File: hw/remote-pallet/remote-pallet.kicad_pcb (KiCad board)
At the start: 2 copper layers, 74 parts, among them M0 E-MATCH, M1 E-MATCH, M2 E-MATCH, M3 E-MATCH, M4 E-MATCH, M5 E-MATCH, M6 E-MATCH, M7 E-MATCH, Q1 Q_PMOS_DGS, Q10 Q_PMOS_DGS, Q11 Q_NMOS_DGS, Q12 Q_PMOS_DGS, Q13 Q_NMOS_DGS, Q14 Q_PMOS_DGS, Q15 Q_NMOS_DGS, Q16 Q_PMOS_DGS, Q17 Q_NMOS_DGS, Q2 Q_PMOS_DGS, Q3 Q_NMOS_DGS, Q4 Q_PMOS_DGS, Q5 Q_NMOS_DGS, Q6 Q_PMOS_DGS, Q7 Q_NMOS_DGS, Q8 Q_PMOS_DGS, Q9 Q_NMOS_DGS, SW1 Power, SW2 Arm Hardware, U1 LM1084IS-3.3/NOPB, U2 PHOTON, U3 LM1084IS-3.3/NOPB

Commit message: updating schematic and pcb
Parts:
- D1, D10, D11, D12, D13, D14, D15, D16, D2, D3, D4, D5, D6, D7, D8, D9, R12, R15, R18, R21, R24, R27, R30, R9: moved to B.Cu
- Q1: value Q_PMOS_DGS -> EMatch Test; footprint TO_SOT_Packages_SMD:TO-252-2Lead -> TO_SOT_Packages_SMD:SOT-23
- U1: value LM1084IS-3.3/NOPB -> Photon Power
- U3: value LM1084IS-3.3/NOPB -> Armed Sense
- moved D10 217.0 mm to (3.81, 194.3)
- moved D4 214.7 mm to (3.81, 203.2)
- moved D12 214.5 mm to (3.81, 189.2)
- moved D6 212.0 mm to (3.81, 199.4)
- moved D14 207.3 mm to (3.81, 185.4)
- moved D16 200.4 mm to (3.81, 179.1)
- moved R32 189.4 mm to (14.0, 43.2), turned to 90 degrees
- moved R31 185.2 mm to (16.5, 43.2), turned to 270 degrees
- moved R29 178.5 mm to (14.0, 57.1), turned to 90 degrees
- moved R28 171.5 mm to (16.5, 57.1), turned to 90 degrees
- moved D2 169.9 mm to (5.08, 174.0)
- moved R22 141.6 mm to (16.5, 83.8), turned to 90 degrees
- moved R20 137.2 mm to (53.3, 36.8), turned to 270 degrees
- moved R9 135.1 mm to (44.5, 205.7)
- moved R26 128.9 mm to (14.0, 69.8), turned to 90 degrees
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
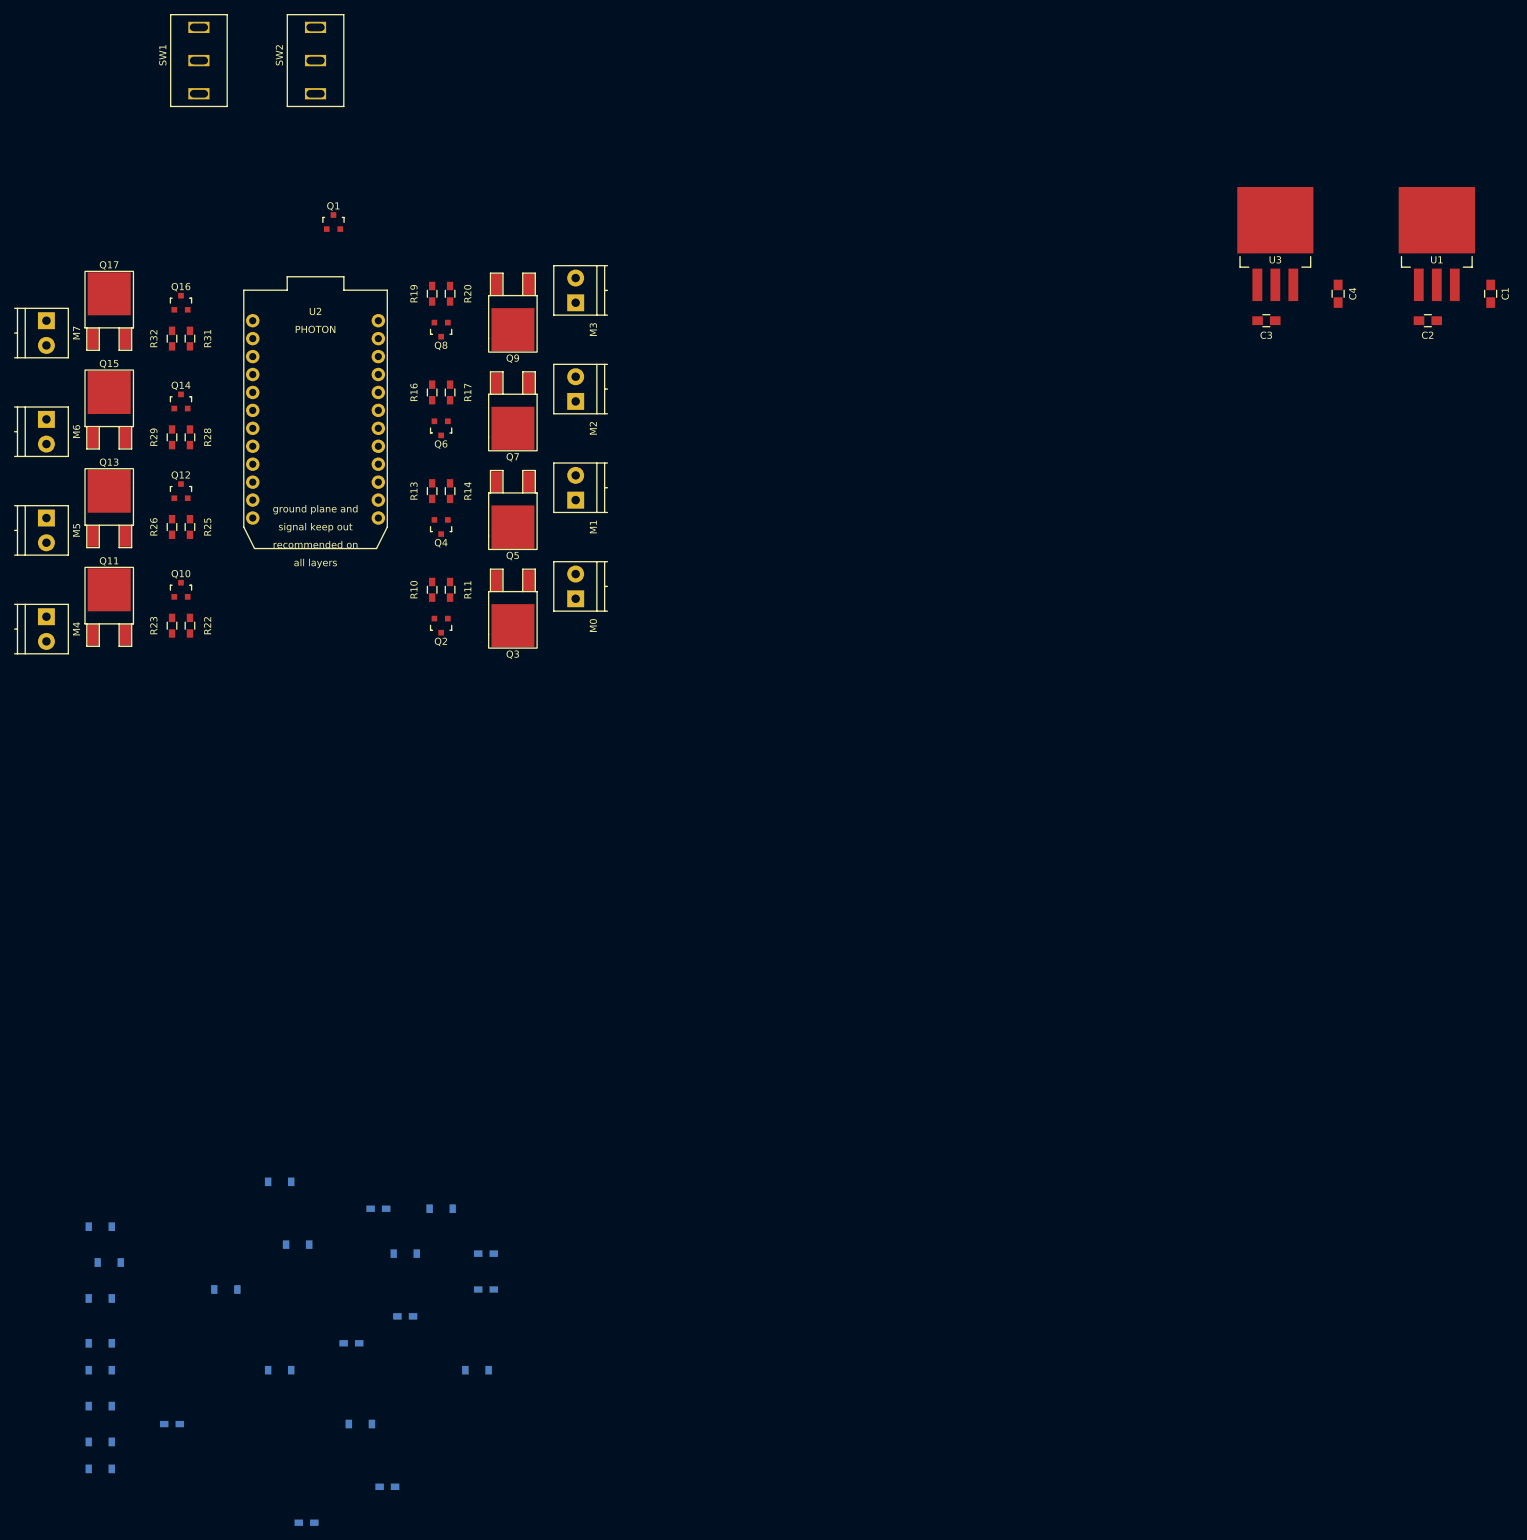
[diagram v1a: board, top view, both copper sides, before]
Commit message: adding some new footprints, laying out board
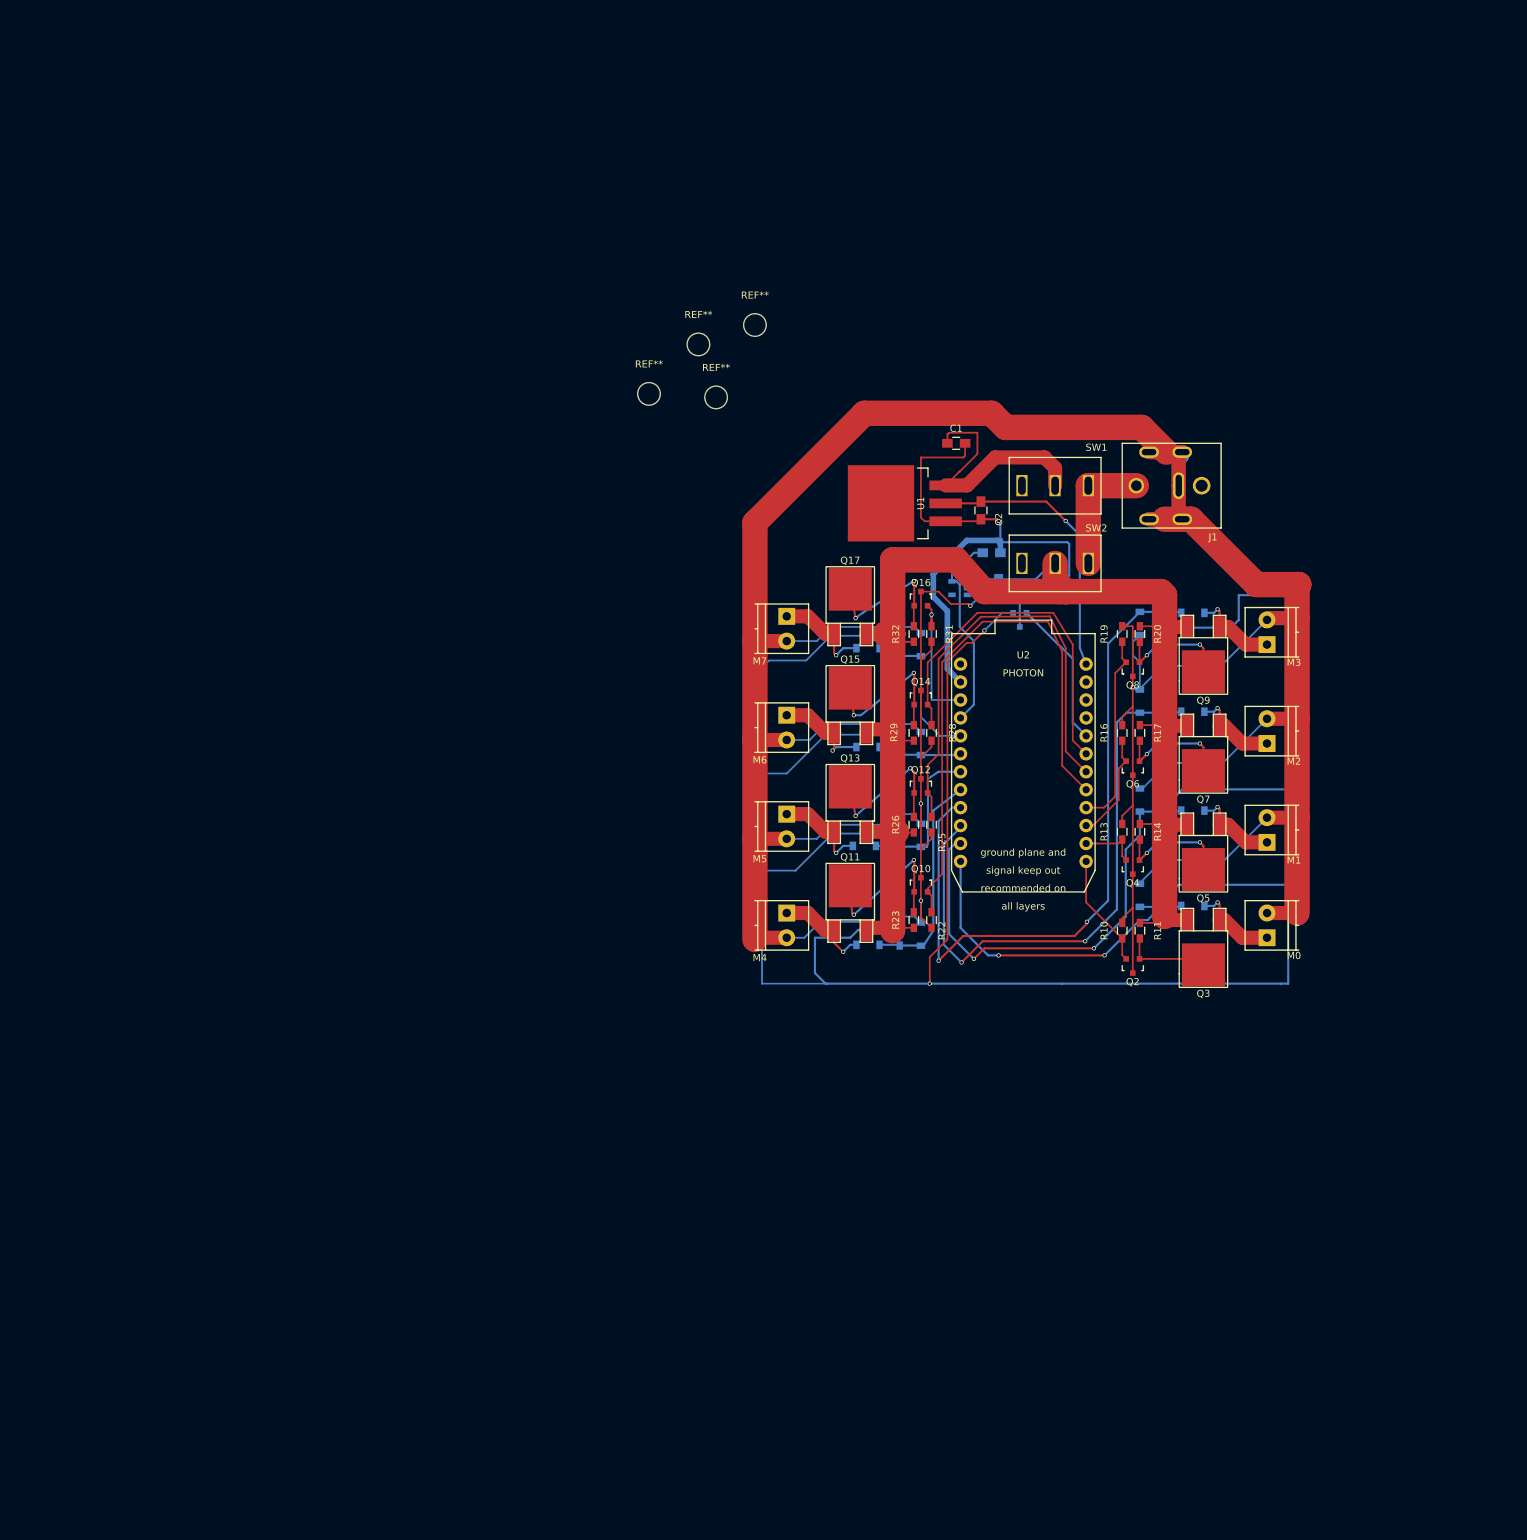
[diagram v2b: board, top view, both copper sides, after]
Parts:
- added J1: Power, PJ-082BH-Barrel-Connector:PJ-082BH-Barrel-Connector, F.Cu at (162.5, 64.0)
- added REF**: MountingHole_3.2mm_M3, Mounting_Holes:MountingHole_3.2mm_M3, F.Cu at (81.5, 51.0)
- added REF**: MountingHole_3.2mm_M3, Mounting_Holes:MountingHole_3.2mm_M3, F.Cu at (88.5, 44.0)
- added REF**: MountingHole_3.2mm_M3, Mounting_Holes:MountingHole_3.2mm_M3, F.Cu at (96.5, 41.2)
- added REF**: MountingHole_3.2mm_M3, Mounting_Holes:MountingHole_3.2mm_M3, F.Cu at (91.0, 51.5)
- C3: value 10uF -> 0.47uF; moved to B.Cu
- C4, Q1: moved to B.Cu
- U3: footprint TO_SOT_Packages_SMD:TO-263-3Lead -> TO_SOT_Packages_SMD:SOT-23-5; moved to B.Cu
- moved D6 186.1 mm to (158.5, 96.0), turned to 180 degrees
- moved D4 180.6 mm to (158.5, 110.0), turned to 180 degrees
- moved D2 161.5 mm to (158.5, 123.5), turned to 180 degrees
- moved D7 160.1 mm to (151.0, 83.5), turned to 270 degrees
- moved D8 155.1 mm to (158.5, 82.0), turned to 180 degrees
- moved D1 154.5 mm to (151.0, 122.0), turned to 90 degrees
- moved R30 150.6 mm to (117.0, 87.0), turned to 90 degrees
- moved R18 145.5 mm to (154.0, 83.0), turned to 270 degrees
- moved D16 142.4 mm to (112.5, 87.0)
- moved D3 141.4 mm to (151.0, 108.5), turned to 90 degrees
- moved D14 137.6 mm to (112.5, 101.0)
- moved R9 137.6 mm to (154.0, 122.5), turned to 90 degrees
- moved SW1 135.3 mm to (139.0, 64.0), turned to 90 degrees
- moved D5 133.3 mm to (151.0, 94.5), turned to 90 degrees
- moved D12 131.2 mm to (112.0, 115.0)
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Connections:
- C4 pad 1: /ematch-0/EMATCH_VCC -> /ematch-0/VCC
- D10 pad 1: /ematch-0/EMATCH_VCC -> /ematch-4/EMATCH_VCC
- D12 pad 1: /ematch-0/EMATCH_VCC -> /ematch-5/EMATCH_VCC
- D14 pad 1: /ematch-0/EMATCH_VCC -> /ematch-6/EMATCH_VCC
- D16 pad 1: /ematch-0/EMATCH_VCC -> /ematch-7/EMATCH_VCC
- D4 pad 1: /ematch-0/EMATCH_VCC -> /ematch-1/EMATCH_VCC
- D6 pad 1: /ematch-0/EMATCH_VCC -> /ematch-2/EMATCH_VCC
- D8 pad 1: /ematch-0/EMATCH_VCC -> /ematch-3/EMATCH_VCC
- M1 pad 1: /ematch-0/EMATCH_VCC -> /ematch-1/EMATCH_VCC
- M2 pad 1: /ematch-0/EMATCH_VCC -> /ematch-2/EMATCH_VCC
- M3 pad 1: /ematch-0/EMATCH_VCC -> /ematch-3/EMATCH_VCC
- M4 pad 1: /ematch-0/EMATCH_VCC -> /ematch-4/EMATCH_VCC
- M5 pad 1: /ematch-0/EMATCH_VCC -> /ematch-5/EMATCH_VCC
- M6 pad 1: /ematch-0/EMATCH_VCC -> /ematch-6/EMATCH_VCC
- M7 pad 1: /ematch-0/EMATCH_VCC -> /ematch-7/EMATCH_VCC
- Q11 pad 1: /ematch-0/EMATCH_VCC -> /ematch-4/EMATCH_VCC
- Q11 pad 3: 12V -> /ematch-0/VCC
- Q13 pad 1: /ematch-0/EMATCH_VCC -> /ematch-5/EMATCH_VCC
- Q13 pad 3: 12V -> /ematch-0/VCC
- Q15 pad 1: /ematch-0/EMATCH_VCC -> /ematch-6/EMATCH_VCC
- Q15 pad 3: 12V -> /ematch-0/VCC
- Q17 pad 1: /ematch-0/EMATCH_VCC -> /ematch-7/EMATCH_VCC
- Q17 pad 3: 12V -> /ematch-0/VCC
- Q3 pad 3: 12V -> /ematch-0/VCC
- Q5 pad 1: /ematch-0/EMATCH_VCC -> /ematch-1/EMATCH_VCC
- Q5 pad 3: 12V -> /ematch-0/VCC
- Q7 pad 1: /ematch-0/EMATCH_VCC -> /ematch-2/EMATCH_VCC
- Q7 pad 3: 12V -> /ematch-0/VCC
- Q9 pad 1: /ematch-0/EMATCH_VCC -> /ematch-3/EMATCH_VCC
- Q9 pad 3: 12V -> /ematch-0/VCC
- R11 pad 1: 12V -> /ematch-0/VCC
- R14 pad 1: 12V -> /ematch-0/VCC
- R17 pad 1: 12V -> /ematch-0/VCC
- R20 pad 1: 12V -> /ematch-0/VCC
- R23 pad 1: 12V -> /ematch-0/VCC
- R26 pad 1: 12V -> /ematch-0/VCC
- R29 pad 1: 12V -> /ematch-0/VCC
- R32 pad 1: 12V -> /ematch-0/VCC
- SW2 pad 2: /ematch-0/EMATCH_VCC -> /ematch-0/VCC
- U2 pad 1: Net-(U2-Pad1) -> (no net)
- U2 pad 20: Fire7 -> SenseSwitch
- U2 pad 22: Net-(U2-Pad22) -> (no net)
- U2 pad 23: Net-(U2-Pad23) -> (no net)
- U2 pad 3: SenseSwitch -> Fire7
- U3 pad 1: GND -> /ematch-0/VCC
- U3 pad 2: Armed -> GND
- U3 pad 3: /ematch-0/EMATCH_VCC -> (no net)
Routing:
- net GND: track 0.00 -> 661.1 mm, vias 0 -> 5
- net VCCsense: track 0.00 -> 377.1 mm, vias 0 -> 2
- net /ematch-0/VCC: track 0.00 -> 224.3 mm
- net Sense3: track 0.00 -> 100.0 mm, vias 0 -> 2
- net Sense2: track 0.00 -> 82.7 mm, vias 0 -> 2
- net Fire4: track 0.00 -> 79.5 mm
- net Fire5: track 0.00 -> 65.2 mm
- net Sense1: track 0.00 -> 64.5 mm, vias 0 -> 2
- net 3.3V: track 0.00 -> 51.5 mm, vias 0 -> 1
- net Fire6: track 0.00 -> 51.3 mm
- net Sense0: track 0.00 -> 48.2 mm, vias 0 -> 2
- net Net-(C1-Pad1): track 0.00 -> 35.2 mm
- net Sense4: track 0.00 -> 30.7 mm
- net Armed: track 0.00 -> 28.4 mm
- net Fire3: track 0.00 -> 27.5 mm
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
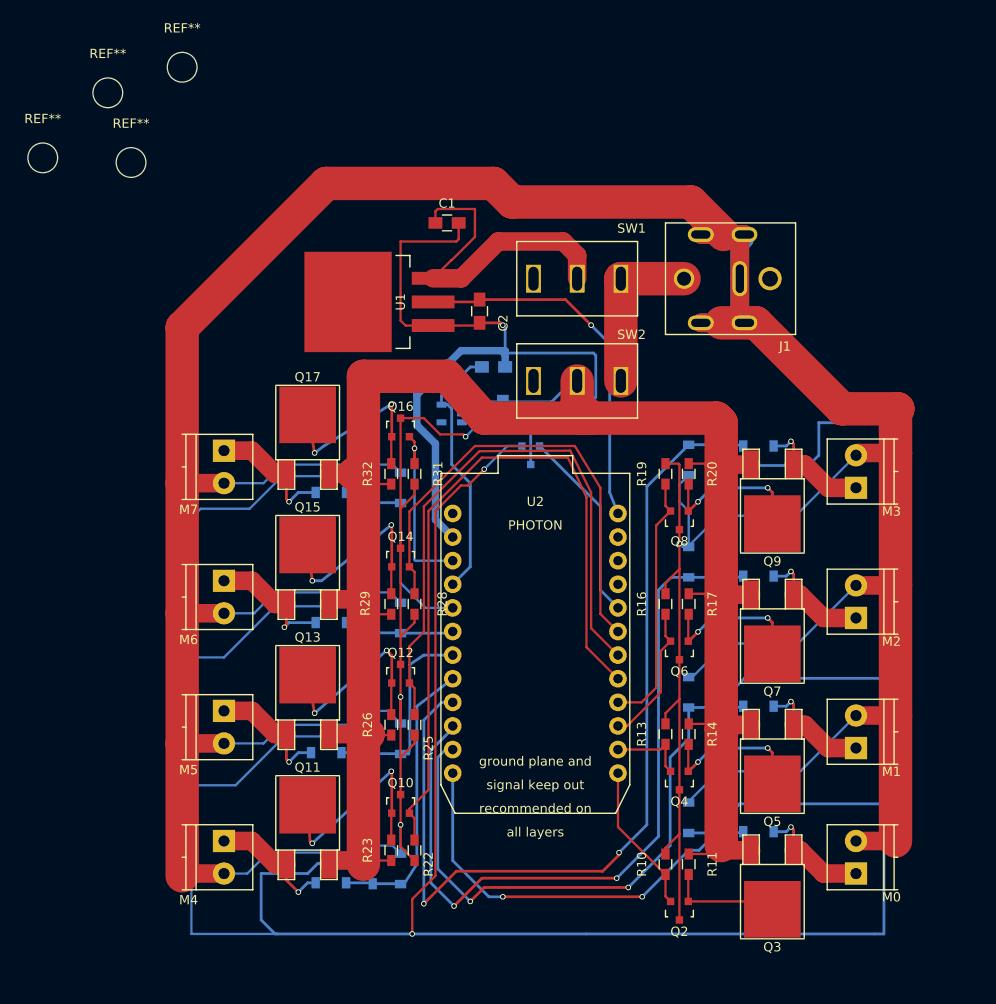
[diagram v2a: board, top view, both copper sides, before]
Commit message: changes to layout adding debug LEDs
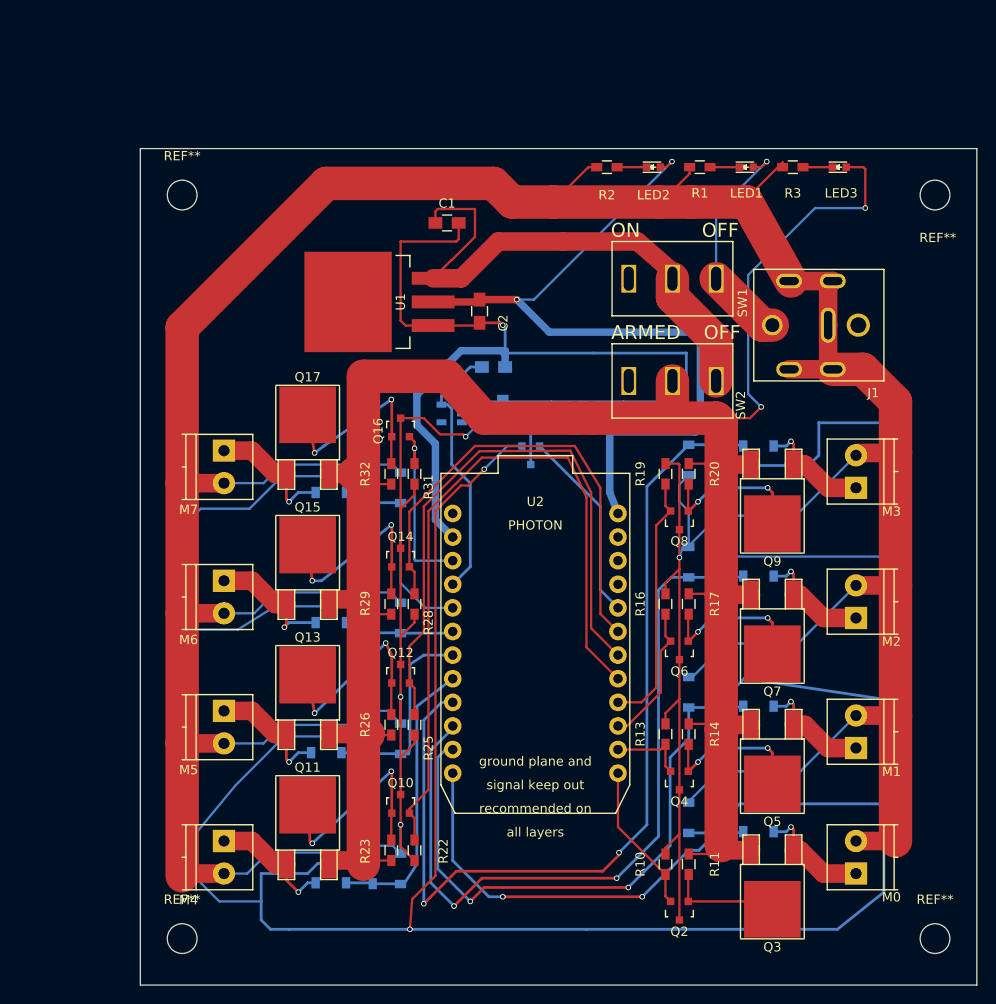
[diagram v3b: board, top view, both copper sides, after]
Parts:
- removed the REF** at (81.5, 51.0)
- removed the REF** at (88.5, 44.0)
- removed the REF** at (96.5, 41.2)
- removed the REF** at (91.0, 51.5)
- added LED1: Battery, LEDs:LED_0603, F.Cu at (157.2, 52.0)
- added LED2: 3.3, LEDs:LED_0603, F.Cu at (147.2, 52.0)
- added LED3: Armed, LEDs:LED_0603, F.Cu at (167.2, 52.0)
- added R1: 600, Resistors_SMD:R_0603_HandSoldering, F.Cu at (152.2, 52.0)
- added R2: 165, Resistors_SMD:R_0603_HandSoldering, F.Cu at (142.2, 52.0)
- added R3: 600, Resistors_SMD:R_0603_HandSoldering, F.Cu at (162.2, 52.0)
- added REF**: MountingHole_3.2mm_M3, Mounting_Holes:MountingHole_3.2mm_M3, F.Cu at (96.5, 55.0)
- added REF**: MountingHole_3.2mm_M3, Mounting_Holes:MountingHole_3.2mm_M3, F.Cu at (177.5, 55.0)
- added REF**: MountingHole_3.2mm_M3, Mounting_Holes:MountingHole_3.2mm_M3, F.Cu at (96.5, 135.0)
- added REF**: MountingHole_3.2mm_M3, Mounting_Holes:MountingHole_3.2mm_M3, F.Cu at (177.5, 135.0)
- moved J1 10.7 mm to (172.0, 69.0)
- moved SW1 10.2 mm to (149.2, 64.0)
- moved SW2 10.2 mm to (149.2, 75.0)
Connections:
- C1 pad 1: Net-(C1-Pad1) -> 12VSwitched
- SW1 pad 2: Net-(C1-Pad1) -> 12VSwitched
- SW2 pad 1: 12V -> 12VSwitched
- U1 pad 3: Net-(C1-Pad1) -> 12VSwitched
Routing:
- net 12VSwitched: track 0.00 -> 56.9 mm
- net /ematch-0/VCC: track 224.3 -> 279.1 mm, vias 0 -> 2
- net 3.3V: track 51.5 -> 95.8 mm, vias 1 -> 2
- net Net-(C1-Pad1): track 35.2 -> 0.00 mm
- net GND: track 661.1 -> 678.2 mm
- net VCCsense: track 377.1 -> 385.7 mm
- net 12V: track 17.8 -> 24.7 mm, vias 0 -> 1
- net Net-(LED3-Pad1): track 0.00 -> 3.15 mm
- net Net-(LED2-Pad1): track 0.00 -> 3.15 mm
- net Net-(LED1-Pad1): track 0.00 -> 3.15 mm
- net Net-(Q12-Pad1): track 21.6 -> 22.8 mm
- net Net-(Q16-Pad1): track 20.4 -> 21.2 mm
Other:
- board outline added: 90 x 90 mm
- board text added: "ARMED"
- board text added: "OFF"
- board text added: "ON"
